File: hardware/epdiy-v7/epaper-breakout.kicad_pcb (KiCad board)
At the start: 4 copper layers, 100 x 55 mm, 116 parts, among them J1 USB_C_Receptacle_USB2.0, J2 EXTENSION_HEADER, J3 ESP_HEADER, J5 CONN_BAT, Q1 AO3401A, Q3 MMBT3904, Q4 MMBT3904, U1 MCP1700-3302E_SOT23, U11 TP4056, U2 PCA9535PW, U3 TPS651851RSLR, U4 USBLC6-2P6, U5 CP2102N-Axx-xQFN28, U6 ED078KH6, U7 PCF8563T, U8 ESP32-S3-WROOM-1, Y1 32.768K

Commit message: v7 signal connections
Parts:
- removed R12: 22.1k, Resistor_SMD:R_0603_1608Metric
- removed R13: 47k, Resistor_SMD:R_0603_1608Metric
- removed R17: 1k, Resistor_SMD:R_0603_1608Metric
- removed R25: 10k, Resistor_SMD:R_0603_1608Metric
- added J4: XF2M-3315-1A, epaper-breakout:CONN_ED097OC4, F.Cu at (106.8, 17.2)
- added J6: 8BIT_HEADER, Connector_PinHeader_2.54mm:PinHeader_1x10_P2.54mm_Vertical, F.Cu at (122.5, 50.8)
- added J7: ESP_HDR, Connector_PinHeader_2.54mm:PinHeader_1x12_P2.54mm_Vertical, F.Cu at (64.9, 11.3)
- added U10: ED060XC5, epaper-breakout:X05A20H34G, F.Cu at (106.5, 24.6)
- added U9: CH340C, Package_SO:SOIC-16_3.9x9.9mm_P1.27mm, F.Cu at (44.9, 27.2)
- C14: value 4.7uF -> 1uF
- C21: value 22pF -> 12pF
- C41: value 100nF -> 12pF
- J3: value ESP_HEADER -> USB_HDR; footprint Connector_PinHeader_2.54mm:PinHeader_1x13_P2.54mm_Vertical -> Connector_PinHeader_2.54mm:PinHeader_1x02_P2.54mm_Vertical
- JP2: value RTCCLK_GPIO1 -> RTCINT_GPIO1
- U1: value MCP1700-3302E_SOT23 -> RT9080-33GJ5; footprint Package_TO_SOT_SMD:SOT-23 -> Package_TO_SOT_SMD:TSOT-23-5
- U5: value CP2102N-Axx-xQFN28 -> XC6206PxxxMR; footprint Package_DFN_QFN:QFN-28-1EP_5x5mm_P0.5mm_EP3.35x3.35mm -> Package_TO_SOT_SMD:SOT-23-3
- moved J3 46.8 mm to (27.1, 20.4), turned to 180 degrees
- moved C41 43.3 mm to (81.8, 22.0), turned to -90 degrees
- moved JP2 24.9 mm to (82.5, 51.0)
- moved Y1 22.9 mm to (85.0, 22.6), turned to 0 degrees
- moved C21 22.0 mm to (88.3, 22.0)
- moved R32 19.8 mm to (81.5, 28.5), turned to -90 degrees
- moved U7 15.8 mm to (85.2, 28.6), turned to -90 degrees
- moved R30 14.3 mm to (122.8, 15.3), turned to 0 degrees
- moved R29 13.6 mm to (122.9, 22.9), turned to 0 degrees
- moved C37 13.4 mm to (122.7, 25.0), turned to 0 degrees
- moved C38 12.4 mm to (122.6, 17.2), turned to 0 degrees
- moved U5 11.0 mm to (42.2, 38.8), turned to 180 degrees
- moved Q3 9.02 mm to (51.8, 22.2), turned to 90 degrees
- moved J2 8.34 mm to (31.9, 11.3)
- moved R27 8.12 mm to (122.8, 19.1), turned to 0 degrees
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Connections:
- C13 pad 2: Net-(C13-Pad2) -> VBUS
- C14 pad 1: VBUS -> GND
- C14 pad 2: GND -> /UART_3.3V
- C2 pad 1: GND -> VIN
- C2 pad 2: VIN -> GND
- C41 pad 2: VBUS -> Net-(C41-Pad2)
- C42 pad 2: Net-(C42-Pad2) -> /UART_3.3V
- J3 pad 1: VIN -> /ESP_USB-
- J3 pad 2: 3.3V -> /ESP_USB+
- JP1 pad 1: /GPIO_2 -> /GPIO_1
- JP2 pad 2: /GPIO_1 -> /GPIO_2
- U1 pad 1: GND -> VIN
- U1 pad 2: 3.3V -> GND
- U5 pad 1: unconnected-(U5-Pad1) -> GND
- U5 pad 2: unconnected-(U5-Pad2) -> /UART_3.3V
- U5 pad 3: GND -> VBUS
- U6 pad 8: /EP_STV -> /IO0
- U7 pad 2: Net-(U7-Pad2) -> Net-(C41-Pad2)
- U8 pad 15: /EP_STV -> /GPIO_3
- Y1 pad 2: Net-(U7-Pad2) -> Net-(C41-Pad2)
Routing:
- net /+22V: track 15.9 -> 204.3 mm, vias 2 -> 6
- net /-20V: track 16.2 -> 201.9 mm, vias 2 -> 7
- net /-15V: track 20.3 -> 168.6 mm, vias 0 -> 5
- net /15V: track 66.0 -> 199.5 mm, vias 2 -> 8
- net EPD_VDD: track 14.9 -> 143.9 mm, vias 2 -> 5
- net /EP_VCOM: track 36.8 -> 150.6 mm, vias 2 -> 5
- net /IO0: track 0.00 -> 106.1 mm, vias 0 -> 10
- net /ESP_USB+: track 0.00 -> 104.1 mm, vias 0 -> 1
- net /ESP_USB-: track 0.00 -> 104.1 mm, vias 0 -> 1
- net /EP_MODE: track 0.00 -> 98.9 mm, vias 0 -> 5
- net /SDA: track 0.00 -> 98.1 mm, vias 0 -> 5
- net /SCL: track 0.00 -> 97.7 mm, vias 0 -> 2
- net /BORDER: track 0.00 -> 94.3 mm, vias 0 -> 3
- net /EP_OE: track 0.00 -> 87.4 mm, vias 0 -> 4
- net /USB_RXD: track 0.00 -> 78.4 mm, vias 0 -> 2
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
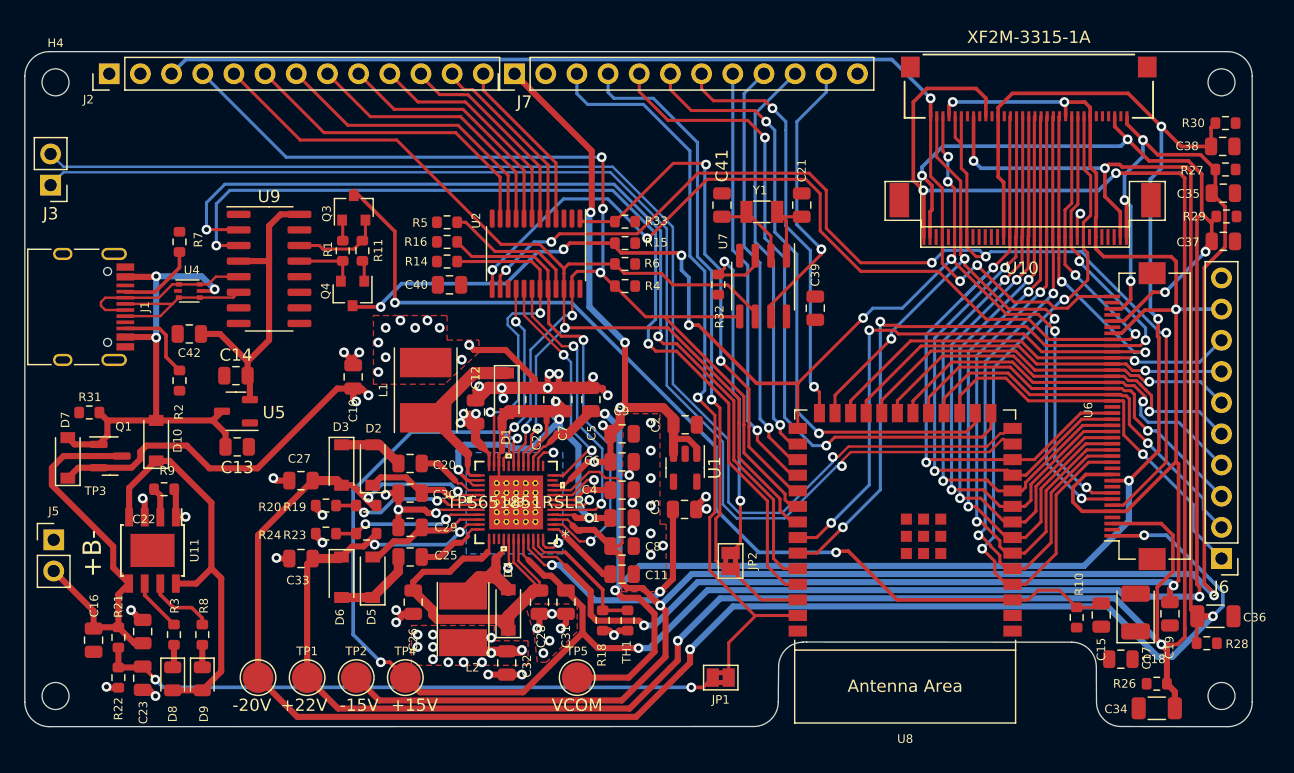
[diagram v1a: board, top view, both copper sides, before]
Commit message: wip: es108fc1 connector
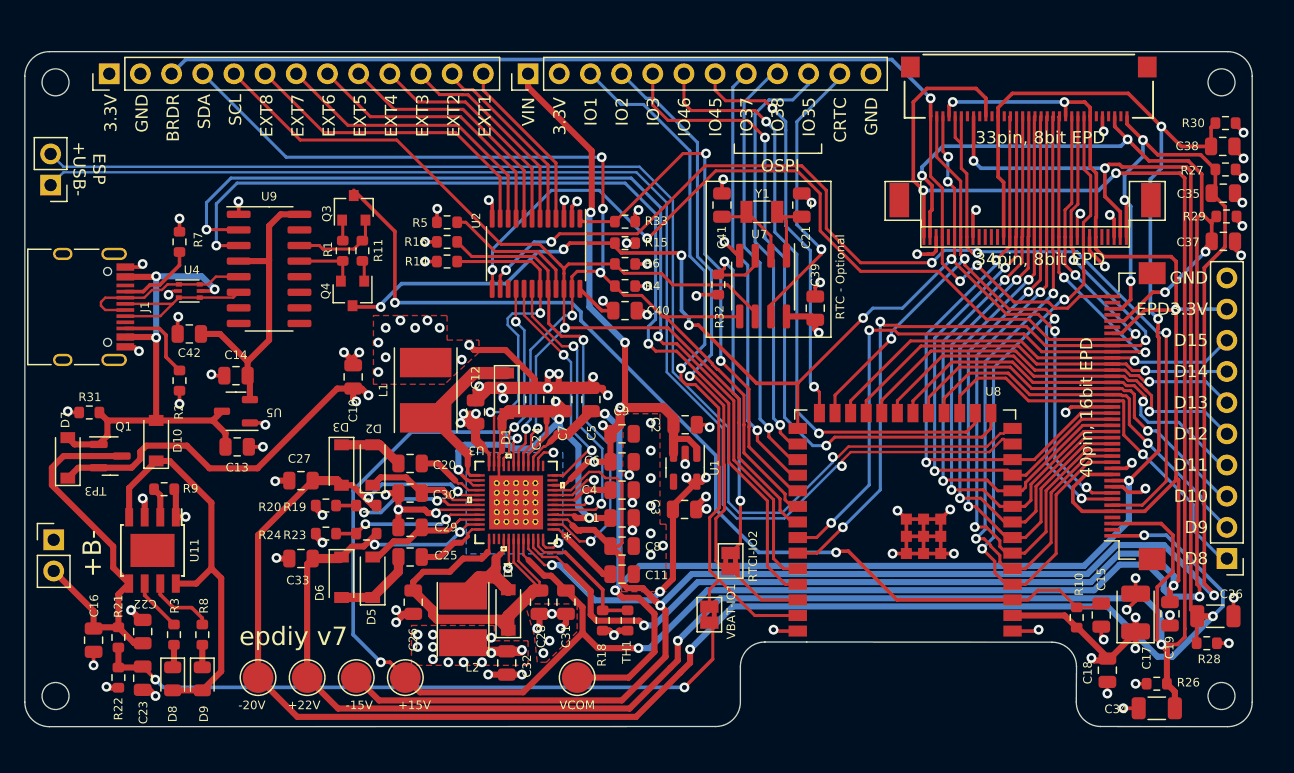
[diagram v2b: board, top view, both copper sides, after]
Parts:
- added REF**: OSHW-Logo2_9.8x8mm_SilkScreen, Symbol:OSHW-Logo2_9.8x8mm_SilkScreen, B.Cu at (117.9, 55.4)
- moved C40 14.5 mm to (73.9, 30.6), turned to 0 degrees
- moved JP1 5.21 mm to (80.8, 55.4), turned to -90 degrees
- moved C18 1.42 mm to (113.2, 59.9), turned to 90 degrees
- moved J7 1.10 mm to (66.0, 11.3)
- moved J6 0.44 mm to (122.9, 50.8)
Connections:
- net /IO0 renamed /EP_STV
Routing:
- net GND: track 82.2 -> 172.4 mm, vias 60 -> 112
- net 3.3V: track 20.7 -> 104.5 mm, vias 2 -> 16
- net Net-(C23-Pad2): track 51.1 -> 54.8 mm
- net /GPIO_1: track 63.5 -> 59.9 mm
- net /D7: track 50.8 -> 47.9 mm
- net EPD_VDD: track 143.9 -> 146.3 mm
- net /15V: track 199.5 -> 201.7 mm
- net /EP_OE: track 87.4 -> 89.6 mm
- net /-15V: track 168.6 -> 170.6 mm
- net /GPIO_35: track 33.3 -> 34.8 mm
- net /USB_TXD: track 77.7 -> 79.2 mm
- net /USB_RXD: track 78.4 -> 79.8 mm
- net /+22V: track 204.3 -> 205.7 mm
- net /ESP_USB+: track 104.1 -> 105.3 mm
- net /ESP_USB-: track 104.1 -> 105.3 mm
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- added copper zone on In2.Cu, net 3.3V
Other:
- outline, holes or cut-outs redrawn
- board text added: "3.3V"
- board text added: "33pin, 8bit EPD"
- board text added: "34pin, 8bit EPD"
- board text added: "40pin, 16bit EPD"
- board text added: "BRDR"
- board text added: "CRTC"
- board text added: "D10"
- board text added: "D11"
- board text added: "D12"
- board text added: "D13"
- board text added: "D14"
- board text added: "D15"
- board text added: "D8"
- board text added: "D9"
- board text added: "EPD3.3V"
- board text added: "ESP +USB-"
- board text added: "EXT1"
- board text added: "EXT2"
- board text added: "EXT3"
- board text added: "EXT4"
- board text added: "EXT5"
- board text added: "EXT6"
- board text added: "EXT7"
- board text added: "EXT8"
- board text added: "GND"
- board text added: "IO1"
- board text added: "IO2"
- board text added: "IO3"
- board text added: "IO35"
- board text added: "IO37"
- board text added: "IO38"
- board text added: "IO45"
- board text added: "IO46"
- board text added: "OSPI"
- board text added: "RTC - Optional"
- board text added: "RTCI-IO2"
- board text added: "SCL"
- board text added: "SDA"
- board text added: "VBAT-IO1"
- board text added: "VIN"
- board text added: "epdiy v7"
- board text added: "epdiy v7 by Valentin Roland 2023 Thanks to the epdiy contributors! For sources and documentation visit https://github.com/vroland/epdiy"
- board text removed: "epdiy v6 by Valentin Roland 2021 Thanks to the epdiy contributors! For sources and documentation visit https://github.com/vroland/epdiy"

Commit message: generate order files
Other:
- rule pad_to_mask_clearance: 0.051 -> 0
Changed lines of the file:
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@@
       (dielectric_constraints no)
     )
-    (pad_to_mask_clearance 0.051)
-    (solder_mask_min_width 0.25)
+    (pad_to_mask_clearance 0)
     (pcbplotparams
-      (layerselection 0x00310fc_ffffffff)
+      (layerselection 0x00010fc_ffffffff)
       (disableapertmacros false)
       (usegerberextensions true)
@@
       (svguseinch false)
       (svgprecision 6)
-      (excludeedgelayer false)
+      (excludeedgelayer true)
       (plotframeref false)
       (viasonmask false)
